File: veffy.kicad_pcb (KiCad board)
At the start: 4 copper layers, 150 parts, among them CN1 XH-2AW_C2908611, J1 SWD, J2 Conn_Coaxial, J3 USB_C_Receptacle_USB2.0_14P, Q1 2N7002, Q2 BFR93A, Q3 2N7002, Q4 BFR93AE6327HTSA1, SW1 SW_Push, SW2 SW_Push, U1 ATSAMD21G18A-A, U10 MC34063AD, U11 AP2112K-3.3, U4 MC3361, U6 TLV9062IDSGR, U7 AD9834, U8 QPA9510, U9 MCP73831-2-OT, Y2 C7527392

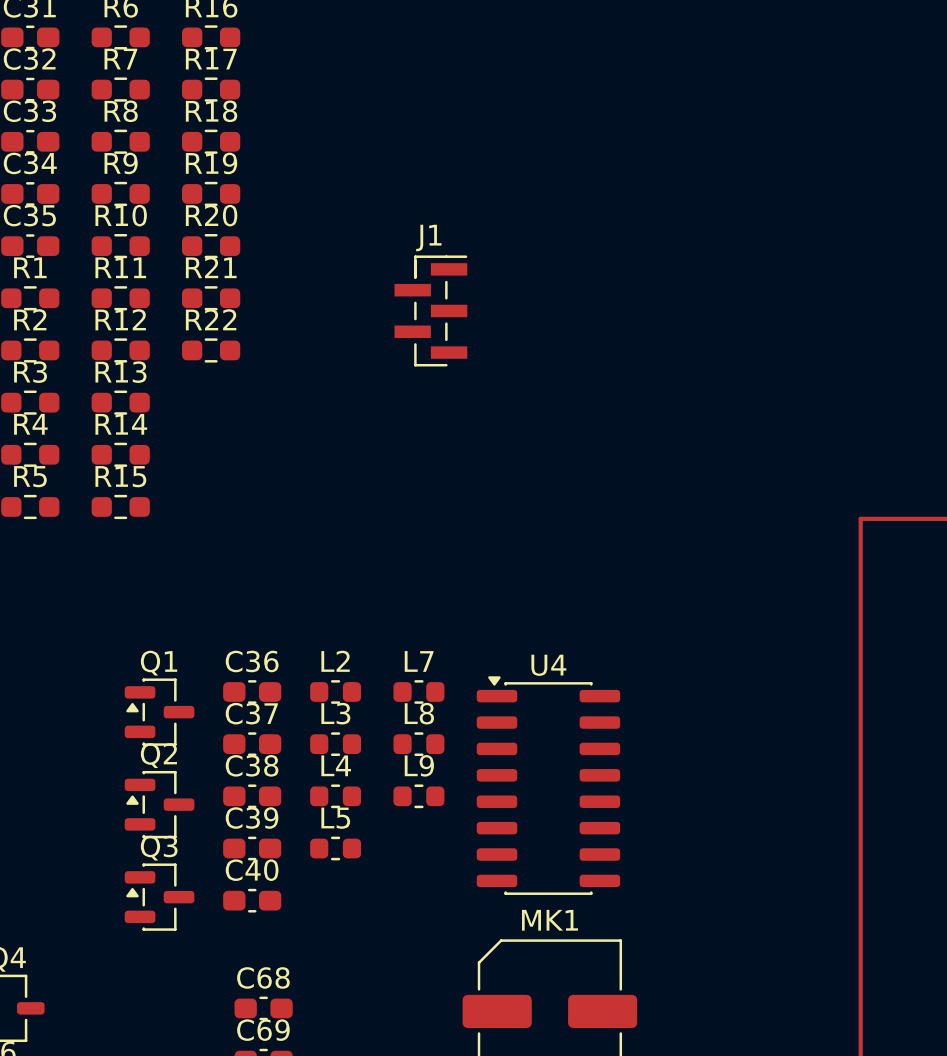
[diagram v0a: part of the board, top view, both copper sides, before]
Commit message: clean up the audio and fix a broken label `FILTER_OUT`
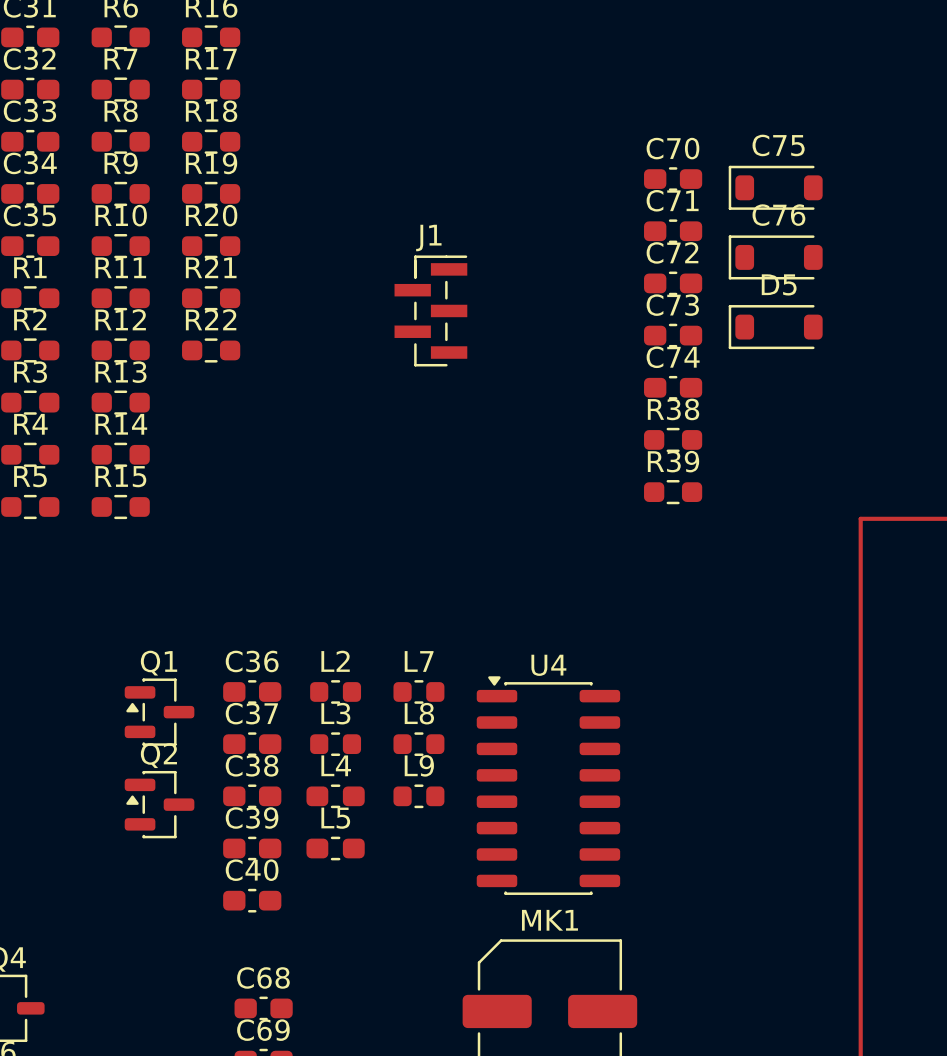
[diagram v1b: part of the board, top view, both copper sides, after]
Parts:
- removed Q3: 2N7002, Package_TO_SOT_SMD:SOT-23
- added C70: 22pF, Capacitor_SMD:C_0603_1608Metric_Pad1.08x0.95mm_HandSolder, F.Cu at (169.3, 69.7)
- added C71: 22pF, Capacitor_SMD:C_0603_1608Metric_Pad1.08x0.95mm_HandSolder, F.Cu at (169.3, 72.2)
- added C72: 100pf, Capacitor_SMD:C_0603_1608Metric_Pad1.08x0.95mm_HandSolder, F.Cu at (169.3, 74.7)
- added C73: 100pF, Capacitor_SMD:C_0603_1608Metric_Pad1.08x0.95mm_HandSolder, F.Cu at (169.3, 77.2)
- added C74: 1nF, Capacitor_SMD:C_0603_1608Metric_Pad1.08x0.95mm_HandSolder, F.Cu at (169.3, 79.7)
- added C75: 0.1uF, Diode_SMD:D_SOD-123, F.Cu at (174.4, 70.1)
- added C76: 0.1uF, Diode_SMD:D_SOD-123, F.Cu at (174.4, 73.4)
- added D5: 1N4148W, Diode_SMD:D_SOD-123, F.Cu at (174.4, 76.8)
- added R38: 4.7K, Resistor_SMD:R_0603_1608Metric_Pad0.98x0.95mm_HandSolder, F.Cu at (169.3, 82.2)
- added R39: 470K, Resistor_SMD:R_0603_1608Metric_Pad0.98x0.95mm_HandSolder, F.Cu at (169.3, 84.7)
- D2: value BAR64-05W -> BAR64-02V
- L4: value 100nH -> 51nH; footprint Inductor_SMD:L_0603_1608Metric -> Inductor_SMD:L_0603_1608Metric_Pad1.05x0.95mm_HandSolder
- L5: value 100nH -> 390nH; footprint Inductor_SMD:L_0603_1608Metric -> Inductor_SMD:L_0603_1608Metric_Pad1.05x0.95mm_HandSolder
- Q1: value 2N7002 -> AO3401A
- R16: value 300 -> 150
- R17: value 300 -> 100K
- R18: value 100K -> 1K
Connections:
- C36 pad 2: Net-(C36-Pad2) -> Net-(D4-K)
- D2 pad 1: RX_RF -> AGND
- D2 pad 2: Net-(Q3-S) -> Net-(D2-A)
- D2 pad 3: Net-(C36-Pad2) -> (no net)
- L4 pad 1: Net-(L4-Pad1) -> Net-(D4-K)
- L4 pad 2: Net-(Q1-D) -> Net-(D2-A)
- Q1 pad 1: RX_EN -> TX_EN
- Q1 pad 2: RX_RF -> DVDD
- R16 pad 1: DVDD -> Net-(Q1-D)
- R17 pad 1: Net-(L4-Pad1) -> TX_EN
- R18 pad 1: RX_EN -> Net-(D5-A)
- R18 pad 2: AGND -> SQUELCH_IN
- R19 pad 1: TX_EN -> SQUELCH_IN
- R19 pad 2: AGND -> DVDD
- U4 pad 10: unconnected-(U4-FILTER_INT-Pad10) -> FILTER_IN
- U4 pad 12: unconnected-(U4-SQUELCH_INT-Pad12) -> SQUELCH_IN
- U4 pad 14: unconnected-(U4-MUTE-Pad14) -> MUTE

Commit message: fix TXCO since it could not output the right DDS and the voltage was wrong
I also fixed the symbol for ERC
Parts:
- removed Y2: C7527392, LCSC:OSC-SMD_4P-L2.0-W1.6-BL_EPSON_TG-5006CJ-19H
- added C77: 1nF, Capacitor_SMD:C_0603_1608Metric_Pad1.08x0.95mm_HandSolder, F.Cu at (186.9, 58.6)
- added C78: 220nF, Capacitor_SMD:C_0603_1608Metric_Pad1.08x0.95mm_HandSolder, F.Cu at (186.9, 61.1)
- added C79: 47nF, Capacitor_SMD:C_0603_1608Metric_Pad1.08x0.95mm_HandSolder, F.Cu at (186.9, 63.6)
- added C80: 4.7uF, Capacitor_SMD:C_0603_1608Metric_Pad1.08x0.95mm_HandSolder, F.Cu at (186.9, 66.1)
- added C81: 1uF, Capacitor_SMD:C_0603_1608Metric_Pad1.08x0.95mm_HandSolder, F.Cu at (186.9, 68.6)
- added C82: 100nF, Capacitor_SMD:C_0603_1608Metric_Pad1.08x0.95mm_HandSolder, F.Cu at (186.9, 71.1)
- added C83: 10nF, Capacitor_SMD:C_0603_1608Metric_Pad1.08x0.95mm_HandSolder, F.Cu at (186.9, 73.6)
- added C84: 100nF, Capacitor_SMD:C_0603_1608Metric_Pad1.08x0.95mm_HandSolder, F.Cu at (186.9, 76.1)
- added C85: 1nF, Capacitor_SMD:C_0603_1608Metric_Pad1.08x0.95mm_HandSolder, F.Cu at (186.9, 78.6)
- added R43: 18K, Resistor_SMD:R_0603_1608Metric_Pad0.98x0.95mm_HandSolder, F.Cu at (186.9, 81.1)
- added R44: 33, Package_TO_SOT_SMD:SOT-553, F.Cu at (190.8, 73.3)
- added R45: 1M, Package_TO_SOT_SMD:SOT-553, F.Cu at (190.8, 76.5)
- added RV1: 22K, Potentiometer_THT:Potentiometer_Alps_RK09K_Single_Vertical, F.Cu at (190.7, 62.0)
- added RV2: 10K, Potentiometer_SMD:Potentiometer_Bourns_3314G_Vertical, F.Cu at (195.5, 75.8)
- added U12: AP2112K-1.8, Package_TO_SOT_SMD:SOT-23-5, F.Cu at (201.1, 74.0)
- added U13: 74LVC1GU04DRL, Package_TO_SOT_SMD:SOT-553, F.Cu at (190.8, 79.7)
- added Y1: 26 MHz, LCSC:OSC-SMD_4P-L2.0-W1.6-BL_EPSON_TG-5006CJ-19H, F.Cu at (200.2, 77.7)
- C35: value 0.1uF -> 1uF
- C75: footprint Diode_SMD:D_SOD-123 -> Capacitor_SMD:C_0603_1608Metric_Pad1.08x0.95mm_HandSolder
- C76: value 0.1uF -> 1nF; footprint Diode_SMD:D_SOD-123 -> Capacitor_SMD:C_0603_1608Metric_Pad1.08x0.95mm_HandSolder
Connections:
- C76 pad 2: unconnected-(C76-Pad2) -> Net-(C76-Pad2)
- R38 pad 2: unconnected-(R38-Pad2) -> Net-(R38-Pad2)

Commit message: re-did most of the RX Audio since I forgot the speaker aaaa
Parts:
- removed R4: 10, Resistor_SMD:R_0603_1608Metric_Pad0.98x0.95mm_HandSolder
- added C86: 1uF, Capacitor_SMD:C_0603_1608Metric_Pad1.08x0.95mm_HandSolder, F.Cu at (158.8, 47.9)
- added C87: 1uF, Capacitor_SMD:C_0603_1608Metric_Pad1.08x0.95mm_HandSolder, F.Cu at (158.8, 50.4)
- added C88: 1uF, Capacitor_SMD:C_0603_1608Metric_Pad1.08x0.95mm_HandSolder, F.Cu at (158.8, 52.9)
- added D4: BAR64-02V, Diode_SMD:D_SOD-523, F.Cu at (150.5, 88.6)
- added J4: Conn_01x02, Connector_JST:JST_PH_B2B-PH-K_1x02_P2.00mm_Vertical, F.Cu at (159.6, 61.9)
- added R40: 3.3K, Resistor_SMD:R_0603_1608Metric_Pad0.98x0.95mm_HandSolder, F.Cu at (158.8, 55.4)
- added R41: 6.8K, Resistor_SMD:R_0603_1608Metric_Pad0.98x0.95mm_HandSolder, F.Cu at (158.8, 57.9)
- added R42: 3.3K, Resistor_SMD:R_0603_1608Metric_Pad0.98x0.95mm_HandSolder, F.Cu at (163.1, 47.9)
- added R46: 20K, Resistor_SMD:R_0603_1608Metric_Pad0.98x0.95mm_HandSolder, F.Cu at (163.1, 50.4)
- added R47: 100K, Resistor_SMD:R_0603_1608Metric_Pad0.98x0.95mm_HandSolder, F.Cu at (163.1, 52.9)
- added R48: 100K, Resistor_SMD:R_0603_1608Metric_Pad0.98x0.95mm_HandSolder, F.Cu at (163.1, 55.4)
- added R49: 47K, Resistor_SMD:R_0603_1608Metric_Pad0.98x0.95mm_HandSolder, F.Cu at (163.1, 57.9)
- added R50: 470K, Resistor_SMD:R_0603_1608Metric_Pad0.98x0.95mm_HandSolder, F.Cu at (167.5, 47.9)
- added R51: 10K, Resistor_SMD:R_0603_1608Metric_Pad0.98x0.95mm_HandSolder, F.Cu at (167.5, 50.4)
- added R52: 10K, Resistor_SMD:R_0603_1608Metric_Pad0.98x0.95mm_HandSolder, F.Cu at (167.5, 52.9)
- added U14: TPA6203A1DRB, Package_DFN_QFN:Texas_DRB0008A, F.Cu at (172.1, 49.1)
- added U2: ADF4112BCPZ, Package_DFN_QFN:QFN-20-1EP_4x4mm_P0.5mm_EP2.5x2.5mm, F.Cu at (152.2, 84.2)
- added U5: TLV9061xDBV, Package_TO_SOT_SMD:SOT-23-5, F.Cu at (167.1, 61.5)
- C19: value 180pF -> 150pF
- C22: value 200uF -> 100nF; footprint Capacitor_SMD:C_0603_1608Metric_Pad1.08x0.95mm_HandSolder -> Diode_SMD:D_SOD-123
- C23: value 0.05uF -> 1uF; footprint Capacitor_SMD:C_0603_1608Metric_Pad1.08x0.95mm_HandSolder -> Diode_SMD:D_SOD-123
- C24: value 10uF -> 100nF; footprint Capacitor_SMD:C_0603_1608Metric_Pad1.08x0.95mm_HandSolder -> Diode_SMD:D_SOD-123
- C42: value 30pF -> 5-30pF
- D2: footprint Package_TO_SOT_SMD:SOT-323_SC-70 -> Diode_SMD:D_SOD-523
- R44, R45: footprint Package_TO_SOT_SMD:SOT-553 -> Resistor_SMD:R_0603_1608Metric_Pad0.98x0.95mm_HandSolder
- U8: footprint Package_DFN_QFN:WQFN-16-1EP_3x3mm_P0.5mm_EP1.6x1.6mm_ThermalVias -> Package_DFN_QFN:VQFN-16-1EP_3x3mm_P0.5mm_EP1.45x1.45mm_ThermalVias
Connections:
- C19 pad 1: Net-(C19-Pad1) -> LC
- C19 pad 2: AGND -> DVDD
- C22 pad 1: Net-(C22-Pad1) -> DVDD
- C22 pad 2: SPEAKER -> AGND
- C23 pad 1: Net-(C23-Pad1) -> AGND
- C23 pad 2: AGND -> Net-(U5-+)
- C24 pad 2: AGND -> AF_VOL
- C42 pad 1: Net-(C19-Pad1) -> LC
- C42 pad 2: AGND -> DVDD
- L2 pad 2: Net-(C19-Pad1) -> DVDD
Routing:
- removed copper zone on B.Cu, net AGND
- removed copper zone on F.Cu, net AGND
- removed copper zone on In1.Cu, net DVDD
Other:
- board outline added: 39.9 x 80.8 mm
